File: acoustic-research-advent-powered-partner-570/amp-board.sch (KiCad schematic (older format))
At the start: 52 parts, among them Q1 BC546B, Q10 BC546B, Q11 BC546B, Q12 BC556B, Q13 BC33740, Q14 BC556B, Q15 KSE3055T, Q16 KSE3055T, Q17 KSE3055T, Q18 BC33740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

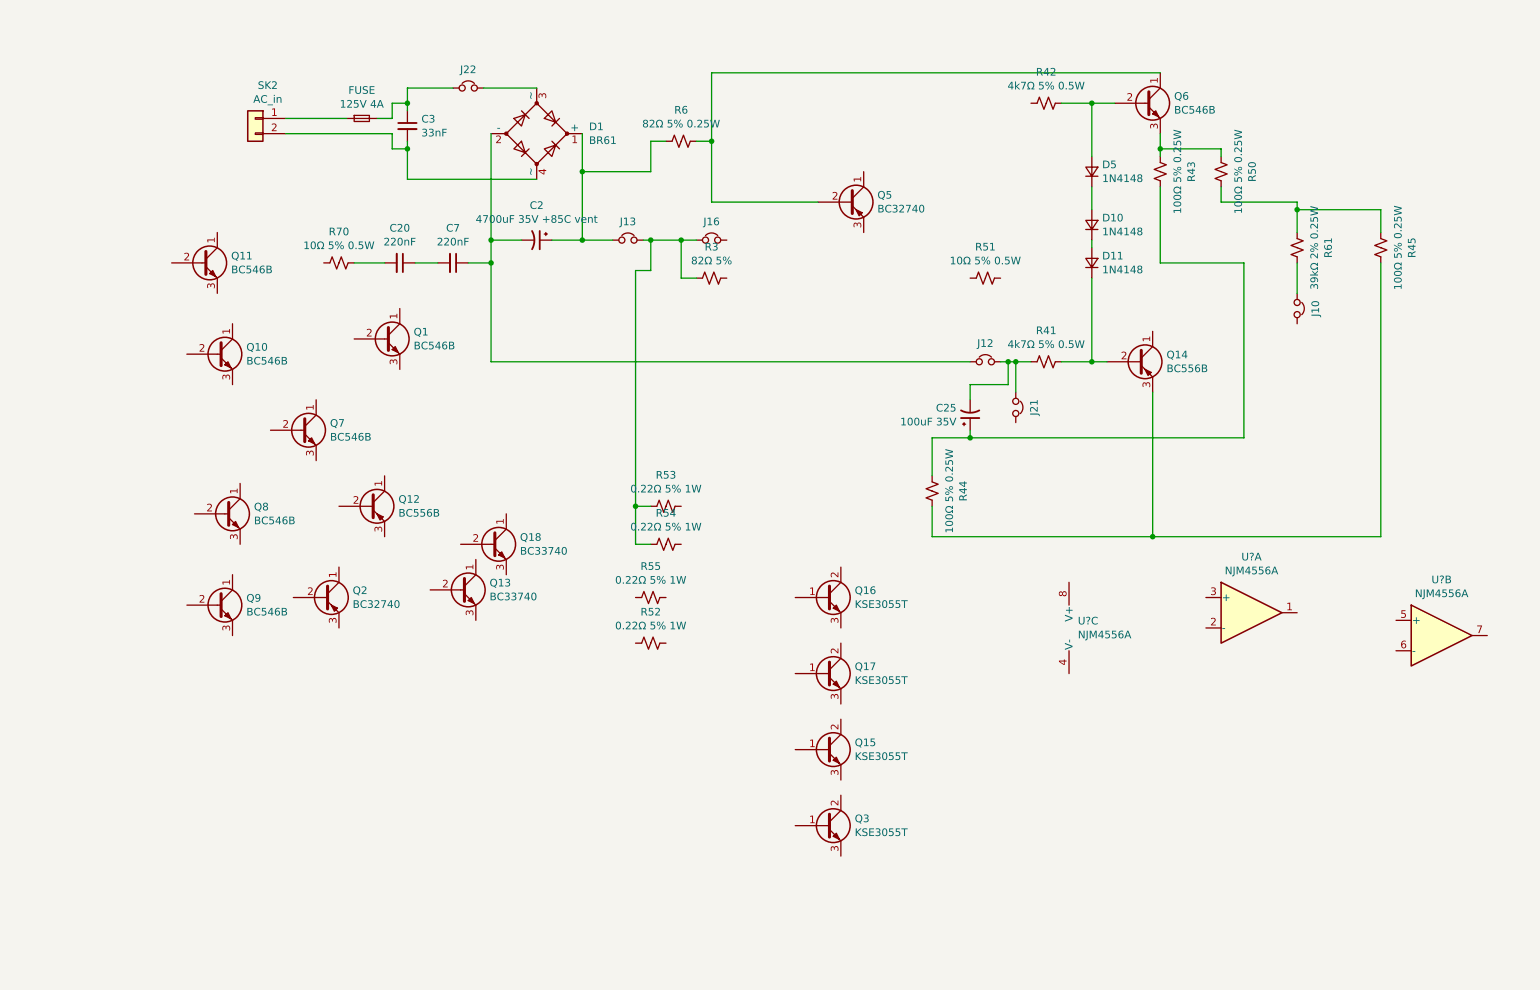
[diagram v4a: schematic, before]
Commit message: hooked up one power transistor
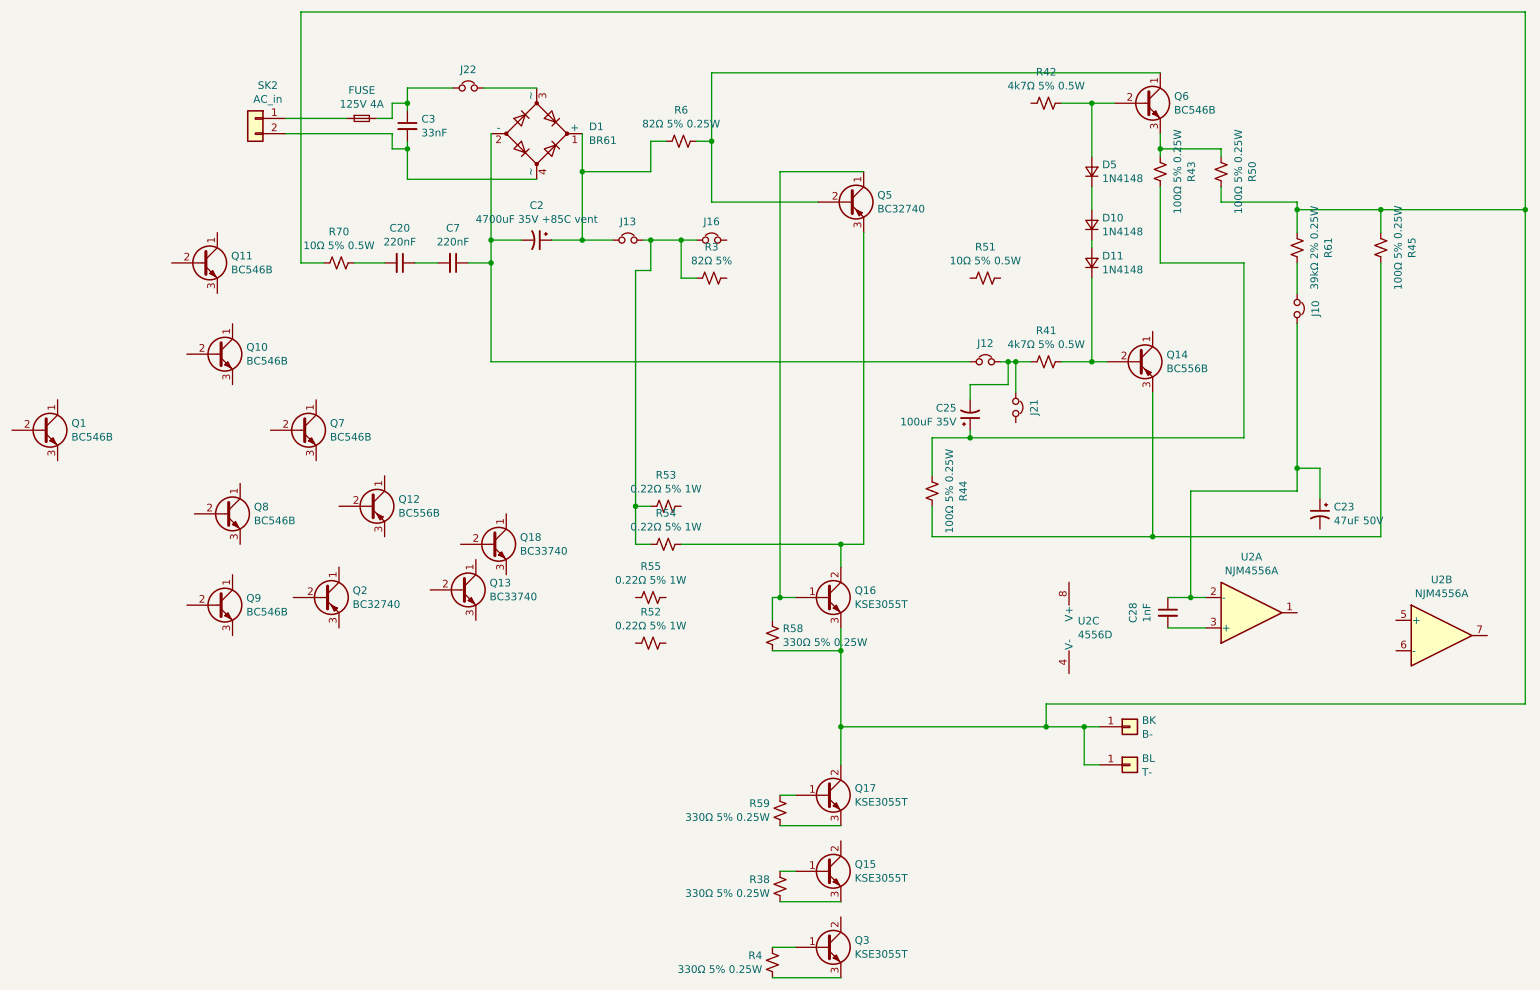
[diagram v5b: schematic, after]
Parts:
- added BK: B-, symbol Connector_Generic:Conn_01x01
- added BL: T-, symbol Connector_Generic:Conn_01x01
- added C23: 47uF 50V, symbol Device:CP1_Small
- added C28: 1nF, symbol Device:C_Small
- added R38, R4, R58, R59: 330Ω 5% 0.25W, symbol Device:R_Small_US
- U2: renamed from U?; value NJM4556A -> 4556D
- gave numbers to parts that had none: 1
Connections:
- net at R70.2: now also Q16.3 (E), Q17.2 (C), R45.2, R50.1, R61.2, BK.1 (Pin_1), BL.1 (Pin_1), R58.1
- net at Q5.1 (C): now also Q16.1 (B), R58.2
- net at Q5.3 (E): now also Q16.2 (C), R54.1
- net at Q17.1 (B): now also R59.2
- net at Q17.3 (E): now also R59.1
- net at Q15.1 (B): now also R38.2
- net at Q15.3 (E): now also R38.1
- net at Q3.1 (B): now also R4.2
- net at Q3.3 (E): now also R4.1
- net at J10.2: now also U2.2 (-), C23.1, C28.1
- net at U2.3 (+): now also C28.2
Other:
- moved on the sheet: Q1, Q15, Q17, Q3

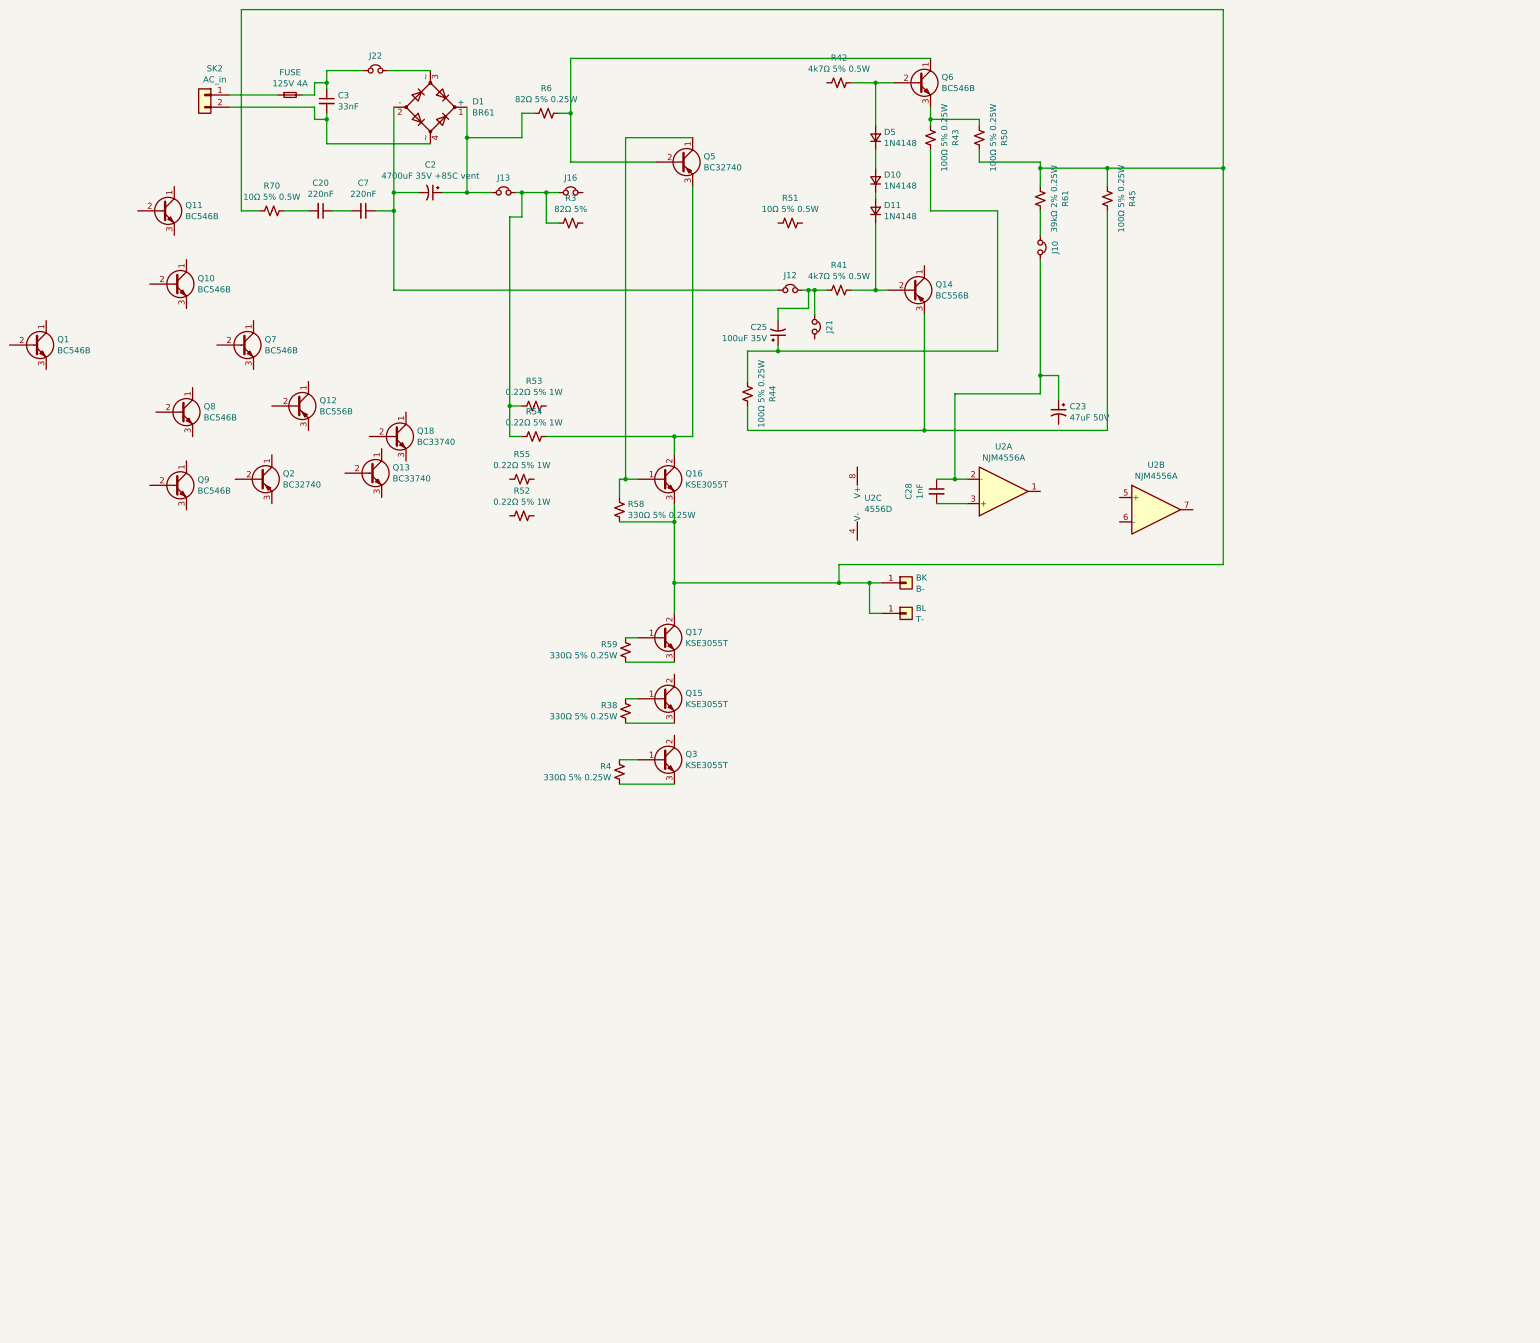
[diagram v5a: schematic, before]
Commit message: I think most of the grounds are connected now
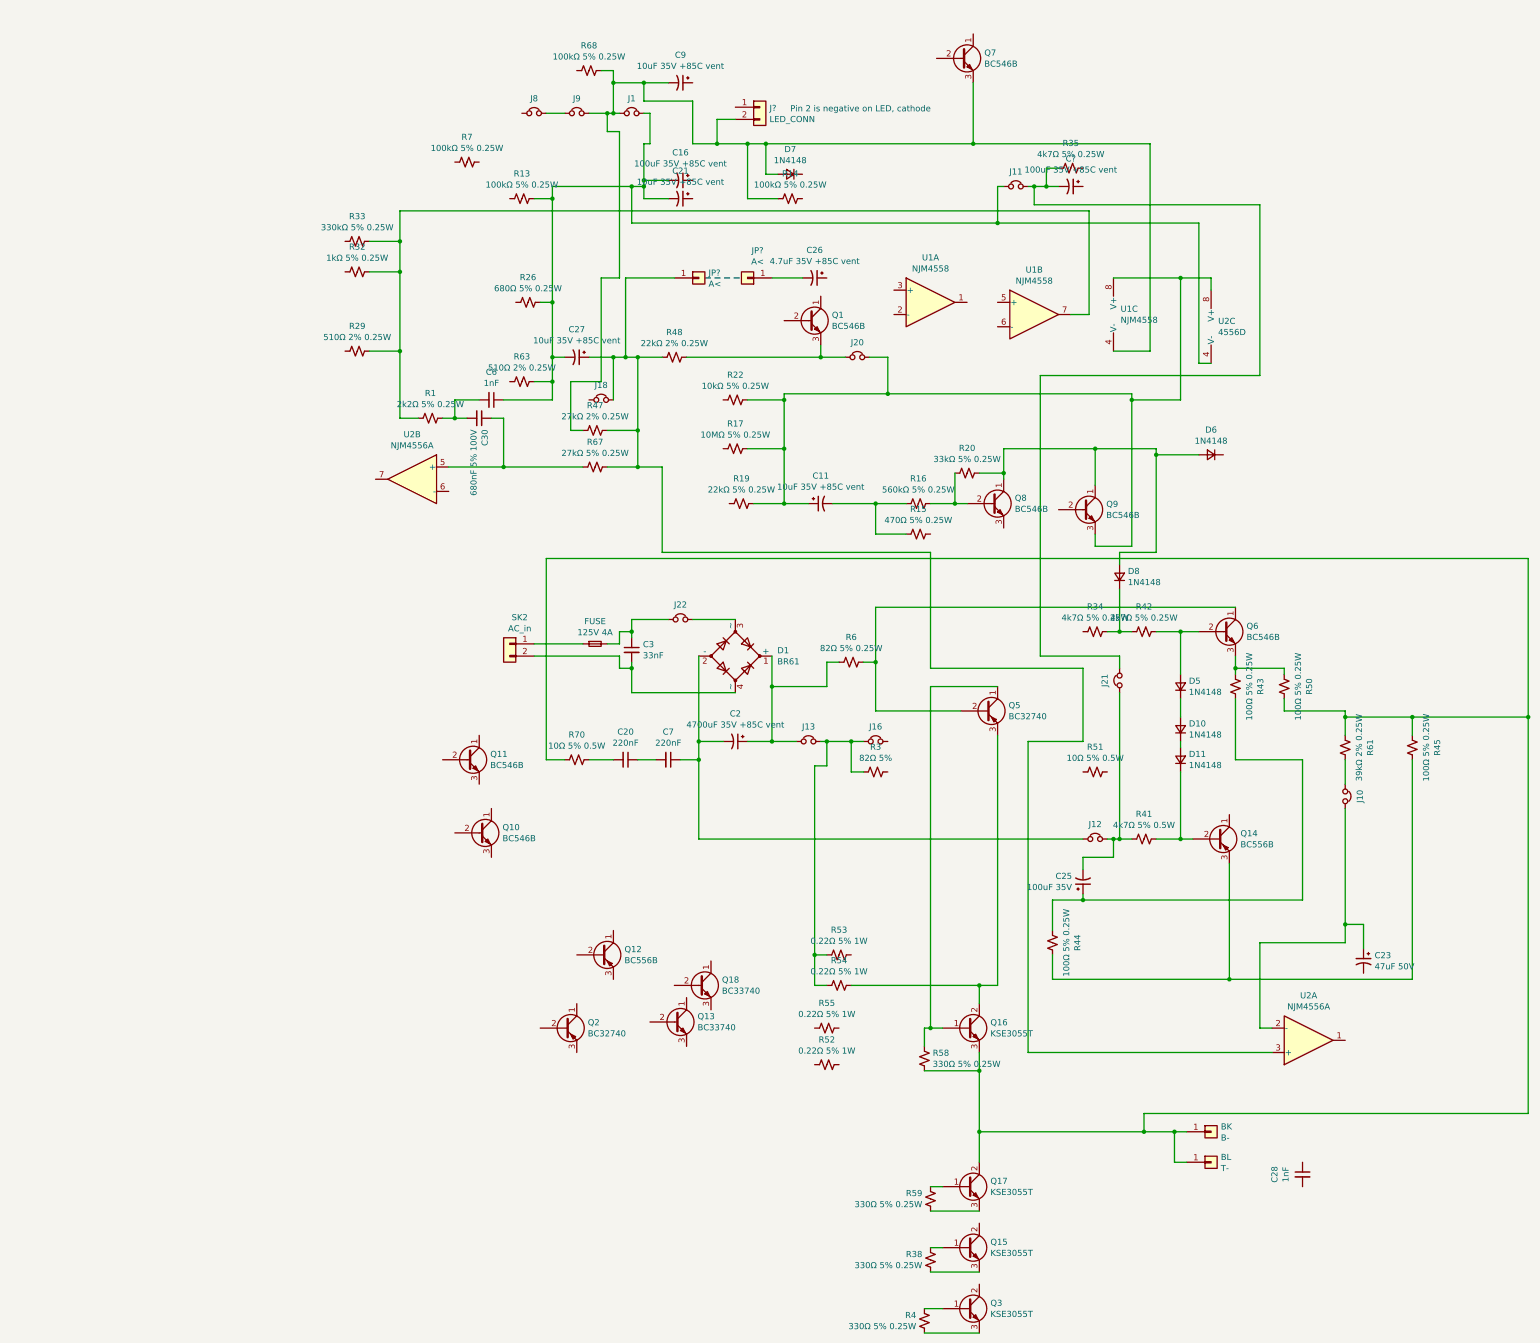
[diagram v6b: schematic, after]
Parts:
- added C11, C21, C27, C9: 10uF 35V +85C vent, symbol Device:CP1_Small
- added C16, C?: 100uF 35V +85C vent, symbol Device:CP1_Small
- added C26: 4.7uF 35V +85C vent, symbol Device:CP1_Small
- added C30: 680nF 5% 100V, symbol Device:C_Small
- added C6: 1nF, symbol Device:C_Small
- added D6, D7, D8: 1N4148, symbol Device:D_Small
- added J1, J11, J18, J20, J8, J9: ~, symbol Device:Jumper_NC_Small
- added J?: LED_CONN, symbol Connector_Generic:Conn_01x02
- added JP? (x2): A<, symbol Connector_Generic:Conn_01x01
- added R1: 2k2Ω 5% 0.25W, symbol Device:R_Small_US
- added R13, R14, R68, R7: 100kΩ 5% 0.25W, symbol Device:R_Small_US
- added R15: 470Ω 5% 0.25W, symbol Device:R_Small_US
- added R16: 560kΩ 5% 0.25W, symbol Device:R_Small_US
- added R17: 10MΩ 5% 0.25W, symbol Device:R_Small_US
- added R19: 22kΩ 5% 0.25W, symbol Device:R_Small_US
- added R20: 33kΩ 5% 0.25W, symbol Device:R_Small_US
- added R22: 10kΩ 5% 0.25W, symbol Device:R_Small_US
- added R26: 680Ω 5% 0.25W, symbol Device:R_Small_US
- added R29, R63: 510Ω 2% 0.25W, symbol Device:R_Small_US
- added R32: 1kΩ 5% 0.25W, symbol Device:R_Small_US
- added R33: 330kΩ 5% 0.25W, symbol Device:R_Small_US
- added R34, R35: 4k7Ω 5% 0.25W, symbol Device:R_Small_US
- added R47: 27kΩ 2% 0.25W, symbol Device:R_Small_US
- added R48: 22kΩ 2% 0.25W, symbol Device:R_Small_US
- added R67: 27kΩ 5% 0.25W, symbol Device:R_Small_US
- added U1: NJM4558, symbol Amplifier_Operational:NJM4558
- R42: value 4k7Ω 5% 0.5W -> 4k7Ω 5% 0.25W
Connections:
- net at R42.2: now also D8.1 (K), R34.1
- net at Q1.3 (E): now also J20.1, R48.1
- net at Q7.3 (E): now also C9.2, D7.2 (A), J1.1, J9.2, J?.2 (Pin_2), R14.2, R47.2, R68.1, U1.4 (V-)
- net at Q8.1 (C): now also Q9.1 (C), D6.2 (A), D8.2 (A), R20.1
- net at Q8.2 (B): now also R16.1, R20.2
- net at Q9.3 (E): now also U2.8 (V+), C11.1, J20.2, R17.1, R19.1, R22.1, U1.8 (V+)
- net at J21.2: now also C?.2, J11.2, R35.2
- net at C23.1, J10.2, U2.2 (-): no longer C28.1
- net at U2.3 (+): now also C27.1, J18.2, JP?.1 (Pin_1), R47.1, R48.2, R67.1; no longer C28.2
- net at U2.5 (+): now also C30.1, R67.2
- net at U2.4 (V-): now also C16.2, C21.2, C27.2, C6.1, J1.2, J11.1, R13.1, R26.1, R63.1
- new net: C11.2, R15.2, R16.2
- new net: R1.2, R29.1, R32.1, R33.1, U1.7
- new net: C26.2, JP?.1 (Pin_1)
- new net: C30.2, C6.2, R1.1
- new net: J8.2, J9.1
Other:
- note added: "Pin 2 is negative on LED, cathode"
- moved on the sheet: BK, BL, C2, C20, C23, C25, C28, C3, C7, D1, D10, D11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

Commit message: finished connections for all large transistors
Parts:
- added C12: 10uF 35V +85C vent, symbol Device:CP1_Small
- added C17, C18: 220nF, symbol Device:C_Small
- added C29: 1uF 35V +85C vent, symbol Device:CP1_Small
- added C31: 3.3uF 50V +85C NP electrolytic, symbol Device:C_Small
- added H?: Heatsink Ground, symbol Mechanical:MountingHole_Pad
- added J14, J15, J17: ~, symbol Device:Jumper_NC_Small
- added J?: JUMPER_TO_INPUT_BOARD, symbol Connector_Generic:Conn_01x06
- added Q4: C546B, Package_TO_SOT_THT:TO-92_Inline, symbol Transistor_BJT:BC546
- added R21: 330kΩ 5% 0.25W, symbol Device:R_Small_US
- added R25: T15A20K T, symbol Device:R_POT_US
- added R36, R37, R39, R40: 100Ω 5% 0.25W, symbol Device:R_Small_US
- added R46: 27kΩ 2% 0.25W, symbol Device:R_Small_US
- added R56, R?: 150Ω 5% 0.25W, symbol Device:R_Small_US
- added R62: 1k5Ω 2% 0.25W, symbol Device:R_Small_US
- added R65: 6k8Ω 5% 0.25W, symbol Device:R_Small_US
- added R94: 10kΩ 2% 0.25W, symbol Device:R_Small_US
- added RD: B+, symbol Connector_Generic:Conn_01x01
- added YL: T+, symbol Connector_Generic:Conn_01x01
- Q1, Q10, Q11, Q6, Q7, Q8, Q9: value BC546B -> C546B
- Q12, Q14: value BC556B -> C556B
- gave numbers to parts that had none: 1
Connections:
- net at C2.2, C7.1, D1.2 (-)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: now also R55.1, H?.1, J14.2
- net at J13.2, J16.1, R53.2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: now also R3.1; no longer R3.2
- net at BK.1 (Pin_1), BL.1 (Pin_1), Q16.3 (E)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: now also Q18.1 (C)
- net at J16.2: now also Q1.1 (C), C29.1, J?.5 (Pin_5), J?.6 (Pin_6), R65.2
- net at R53.1: now also Q2.3 (E), Q3.2 (C)
- net at R55.2: now also Q17.3 (E), R59.1
- net at R52.1: now also J14.1, J15.2, R56.1, R?.1
- net at R52.2: now also Q15.3 (E), R38.1
- net at Q17.1 (B), R59.2: now also Q18.3 (E)
- net at Q15.1 (B), R38.2: now also Q13.3 (E)
- net at Q15.2 (C): now also Q13.1 (C), Q3.3 (E), R4.1, C17.1, C31.1, R37.2, R40.2, R46.1, R94.2, RD.1 (Pin_1)
- net at Q3.1 (B), R4.2: now also Q2.1 (C)
- net at Q14.1 (C): now also Q18.2 (B), R56.2
- net at Q12.1 (C): now also Q13.2 (B), R?.2
- net at Q12.3 (E): now also R36.2, R37.1
- net at Q2.2 (B): now also R3.2, Q4.1 (C)
- net at Q10.3 (E): now also J8.1, Q11.3 (E), C12.2, J?.2 (Pin_2), R21.1, R25.1
- net at R51.1: now also C18.1
- net at R51.2: now also J15.1, J17.1
- net at C23.2: now also R62.1
- net at R63.2: now also R62.2, R94.1
- net at C24.1: now also R36.1, R39.1
- new net: Q4.3 (E), R39.2, R40.1
- new net: C29.2, J17.2, J?.3 (Pin_3), J?.4 (Pin_4)
- new net: C17.2, C18.2
- new net: C31.2, YL.1 (Pin_1)
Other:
- note added: "PIN 6 is White Stripe"
- moved on the sheet: BK, BL, C11, C16, C2, C20, C21, C23, C24, C25, C26, C27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
